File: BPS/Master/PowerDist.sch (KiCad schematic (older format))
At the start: 15 parts, among them J4 CarPowerConnector, U2 RI3-1205S, U3 NCP1117-3.3_SOT223

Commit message: Edited inductor choke in BPS master.
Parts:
- L1: footprint Inductor_SMD:L_0805_2012Metric -> UTSVT_BPS:SRF0905A; symbol Device:L -> utsvt-bps:SRF0905-100Y
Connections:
- wire segments 56 -> 64
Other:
- moved on the sheet: C16, TP1, TP15
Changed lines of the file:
@@
 L utsvt-connectors:CarPowerConnector J4
 U 1 1 5C35F236
-P 2800 3400
-F 0 "J4" H 2850 3750 60  0000 C CNN
-F 1 "CarPowerConnector" H 2500 3650 60  0000 C CNN
-F 2 "UTSVT_Connectors:Molex_MicroFit3.0_1x2xP3.00mm_PolarizingPeg_Vertical" H 2800 3400 60  0001 C CNN
-F 3 "" H 2800 3400 60  0001 C CNN
-	1    2800 3400
-	1    0    0    -1
-$EndComp
-Wire Wire Line
-	3100 3300 3150 3300
-Wire Wire Line
-	3100 3500 3150 3500
-Wire Wire Line
-	3150 3500 3150 3600
+P 2100 3400
+F 0 "J4" H 2150 3750 60  0000 C CNN
+F 1 "CarPowerConnector" H 1800 3650 60  0000 C CNN
+F 2 "UTSVT_Connectors:Molex_MicroFit3.0_1x2xP3.00mm_PolarizingPeg_Vertical" H 2100 3400 60  0001 C CNN
+F 3 "" H 2100 3400 60  0001 C CNN
+	1    2100 3400
+	1    0    0    -1
+$EndComp
+Wire Wire Line
+	2400 3300 2450 3300
+Wire Wire Line
+	2400 3500 2450 3500
+Wire Wire Line
+	2450 3500 2450 3600
 $Comp
 L power:+12V #PWR034
 U 1 1 5C35F2D2
-P 3150 3150
-F 0 "#PWR034" H 3150 3000 50  0001 C CNN
-F 1 "+12V" H 3165 3323 50  0000 C CNN
-F 2 "" H 3150 3150 50  0001 C CNN
-F 3 "" H 3150 3150 50  0001 C CNN
-	1    3150 3150
-	1    0    0    -1
-$EndComp
-Connection ~ 3150 3600
-Wire Wire Line
-	3150 3600 3150 3650
+P 2450 3150
+F 0 "#PWR034" H 2450 3000 50  0001 C CNN
+F 1 "+12V" H 2465 3323 50  0000 C CNN
+F 2 "" H 2450 3150 50  0001 C CNN
+F 3 "" H 2450 3150 50  0001 C CNN
+	1    2450 3150
+	1    0    0    -1
+$EndComp
+Connection ~ 2450 3600
+Wire Wire Line
+	2450 3600 2450 3650
 $Comp
 L Device:C C16
 U 1 1 5C35F7E4
-P 3400 3400
-F 0 "C16" H 3518 3446 50  0000 L CNN
-F 1 "4.7uF" H 3518 3355 50  0000 L CNN
-F 2 "Capacitor_SMD:C_0805_2012Metric" H 3438 3250 50  0001 C CNN
-F 3 "~" H 3400 3400 50  0001 C CNN
-	1    3400 3400
-	1    0    0    -1
-$EndComp
-Wire Wire Line
-	3150 3600 3400 3600
-$Comp
-L Device:L L1
-U 1 1 5C35FFD4
-P 3700 3200
-F 0 "L1" V 3890 3200 50  0000 C CNN
-F 1 "10uH" V 3799 3200 50  0000 C CNN
-F 2 "Inductor_SMD:L_0805_2012Metric" H 3700 3200 50  0001 C CNN
-F 3 "~" H 3700 3200 50  0001 C CNN
-	1    3700 3200
-	0    -1   -1   0
-$EndComp
-Wire Wire Line
-	3150 3150 3150 3200
-Wire Wire Line
-	3150 3200 3400 3200
-Connection ~ 3150 3200
-Wire Wire Line
-	3150 3200 3150 3300
-Wire Wire Line
-	3400 3250 3400 3200
-Connection ~ 3400 3200
-Wire Wire Line
-	3400 3200 3550 3200
-Wire Wire Line
-	3400 3550 3400 3600
-Connection ~ 3400 3600
-Wire Wire Line
-	3400 3600 4000 3600
-Wire Wire Line
-	4000 3200 3850 3200
+P 2700 3400
+F 0 "C16" H 2818 3446 50  0000 L CNN
+F 1 "4.7uF" H 2818 3355 50  0000 L CNN
+F 2 "Capacitor_SMD:C_0805_2012Metric" H 2738 3250 50  0001 C CNN
+F 3 "~" H 2700 3400 50  0001 C CNN
+	1    2700 3400
+	1    0    0    -1
+$EndComp
+Wire Wire Line
+	2450 3600 2700 3600
+Wire Wire Line
+	2450 3150 2450 3200
+Wire Wire Line
+	2450 3200 2700 3200
+Connection ~ 2450 3200
+Wire Wire Line
+	2450 3200 2450 3300
+Wire Wire Line
+	2700 3250 2700 3200
+Connection ~ 2700 3200
+Wire Wire Line
+	2700 3550 2700 3600
+Connection ~ 2700 3600
 Wire Wire Line
 	5200 3700 5200 3600
@@
 L Connector:TestPoint TP1
 U 1 1 5C37D606
-P 3400 3150
-F 0 "TP1" H 3400 3500 50  0000 L CNN
-F 1 "+12V_TP" H 3400 3400 50  0000 L CNN
-F 2 "TestPoint:TestPoint_Keystone_5005-5009_Compact" H 3600 3150 50  0001 C CNN
-F 3 "~" H 3600 3150 50  0001 C CNN
-	1    3400 3150
-	1    0    0    -1
-$EndComp
-Wire Wire Line
-	3400 3150 3400 3200
+P 2700 3150
+F 0 "TP1" H 2700 3500 50  0000 L CNN
+F 1 "+12V_TP" H 2700 3400 50  0000 L CNN
+F 2 "TestPoint:TestPoint_Keystone_5005-5009_Compact" H 2900 3150 50  0001 C CNN
+F 3 "~" H 2900 3150 50  0001 C CNN
+	1    2700 3150
+	1    0    0    -1
+$EndComp
+Wire Wire Line
+	2700 3150 2700 3200
 $Comp
 L Connector:TestPoint TP2
@@
 L power:GNDPWR #PWR036
 U 1 1 5C3F7204
-P 3150 3650
-F 0 "#PWR036" H 3150 3450 50  0001 C CNN
-F 1 "GNDPWR" H 3154 3496 50  0000 C CNN
-F 2 "" H 3150 3600 50  0001 C CNN
-F 3 "" H 3150 3600 50  0001 C CNN
-	1    3150 3650
+P 2450 3650
+F 0 "#PWR036" H 2450 3450 50  0001 C CNN
+F 1 "GNDPWR" H 2454 3496 50  0000 C CNN
+F 2 "" H 2450 3600 50  0001 C CNN
+F 3 "" H 2450 3600 50  0001 C CNN
+	1    2450 3650
 	1    0    0    -1
 $EndComp
@@
 L Connector:TestPoint TP15
 U 1 1 5C82CEA3
-P 3400 3650
-F 0 "TP15" H 3342 3677 50  0000 R CNN
-F 1 "GNDPWR_TP" H 3342 3768 50  0000 R CNN
-F 2 "TestPoint:TestPoint_Keystone_5005-5009_Compact" H 3600 3650 50  0001 C CNN
-F 3 "~" H 3600 3650 50  0001 C CNN
-	1    3400 3650
+P 2700 3650
+F 0 "TP15" H 2642 3677 50  0000 R CNN
+F 1 "GNDPWR_TP" H 2642 3768 50  0000 R CNN
+F 2 "TestPoint:TestPoint_Keystone_5005-5009_Compact" H 2900 3650 50  0001 C CNN
+F 3 "~" H 2900 3650 50  0001 C CNN
+	1    2700 3650
 	-1   0    0    1
 $EndComp
 Wire Wire Line
-	3400 3650 3400 3600
+	2700 3650 2700 3600
+Wire Wire Line
+	3800 3200 4000 3200
+Wire Wire Line
+	2700 3600 4000 3600
+$Comp
+L utsvt-bps:SRF0905-100Y L1
+U 1 1 5C35FFD4
+P 2950 3150
+F 0 "L1" H 3200 3450 50  0000 C CNN
+F 1 "10uH" H 3250 3350 50  0000 C CNN
+F 2 "UTSVT_BPS:SRF0905A" H 2950 3150 50  0001 C CNN
+F 3 "~" H 2950 3150 50  0001 C CNN
+	1    2950 3150
+	1    0    0    -1
+$EndComp
+Wire Wire Line
+	3800 3200 3800 3150
+Wire Wire Line
+	3800 3150 3750 3150
+Wire Wire Line
+	3750 3250 3800 3250
+Wire Wire Line
+	3800 3250 3800 3200
+Connection ~ 3800 3200
+Wire Wire Line
+	2950 3250 2900 3250
+Wire Wire Line
+	2900 3250 2900 3200
+Wire Wire Line
+	2900 3150 2950 3150
+Wire Wire Line
+	2700 3200 2900 3200
+Connection ~ 2900 3200
+Wire Wire Line
+	2900 3200 2900 3150
 $EndSCHEMATC

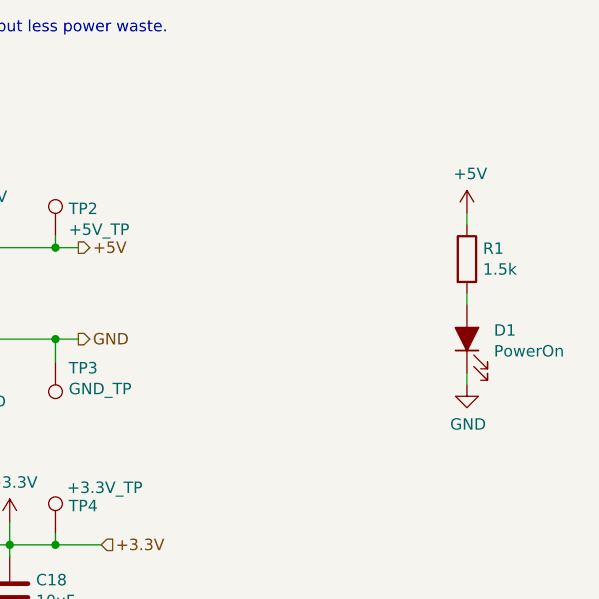
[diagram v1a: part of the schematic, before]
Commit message: Added labels to USB breakout.
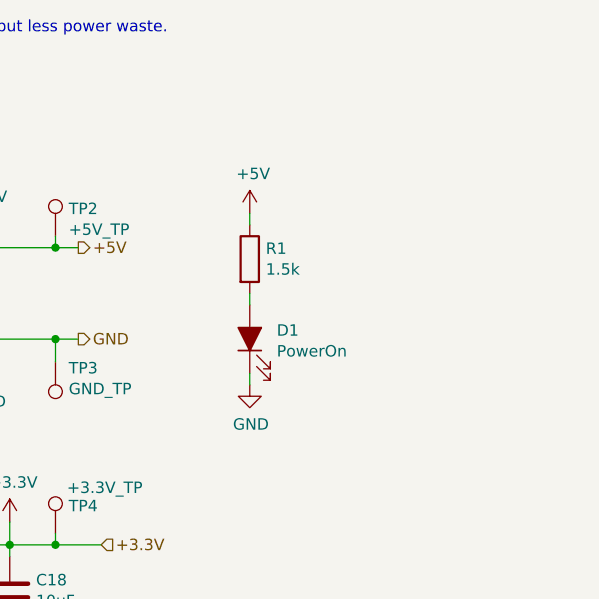
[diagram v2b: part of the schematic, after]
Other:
- moved on the sheet: D1, R1
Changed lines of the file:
@@
 L power:GND #PWR038
 U 1 1 5C58D746
-P 7300 3800
-F 0 "#PWR038" H 7300 3550 50  0001 C CNN
-F 1 "GND" H 7305 3627 50  0000 C CNN
-F 2 "" H 7300 3800 50  0001 C CNN
-F 3 "" H 7300 3800 50  0001 C CNN
-	1    7300 3800
+P 6350 3800
+F 0 "#PWR038" H 6350 3550 50  0001 C CNN
+F 1 "GND" H 6355 3627 50  0000 C CNN
+F 2 "" H 6350 3800 50  0001 C CNN
+F 3 "" H 6350 3800 50  0001 C CNN
+	1    6350 3800
 	1    0    0    -1
 $EndComp
@@
 L Device:LED_ALT D1
 U 1 1 5C58D83E
-P 7300 3600
-F 0 "D1" V 7338 3482 50  0000 R CNN
-F 1 "PowerOn" V 7247 3482 50  0000 R CNN
-F 2 "LED_SMD:LED_0805_2012Metric" H 7300 3600 50  0001 C CNN
-F 3 "~" H 7300 3600 50  0001 C CNN
-F 4 "Green" V 7300 3600 50  0001 C CNN "Color"
-F 5 "APTD2012LCGCK" V 7300 3600 50  0001 C CNN "P/N"
-	1    7300 3600
+P 6350 3600
+F 0 "D1" V 6388 3482 50  0000 R CNN
+F 1 "PowerOn" V 6297 3482 50  0000 R CNN
+F 2 "LED_SMD:LED_0805_2012Metric" H 6350 3600 50  0001 C CNN
+F 3 "~" H 6350 3600 50  0001 C CNN
+F 4 "Green" V 6350 3600 50  0001 C CNN "Color"
+F 5 "APTD2012LCGCK" V 6350 3600 50  0001 C CNN "P/N"
+	1    6350 3600
 	0    -1   -1   0
 $EndComp
@@
 L Device:R R1
 U 1 1 5C58D993
-P 7300 3250
-F 0 "R1" H 7370 3296 50  0000 L CNN
-F 1 "1.5k" H 7370 3205 50  0000 L CNN
-F 2 "Resistor_SMD:R_0805_2012Metric" V 7230 3250 50  0001 C CNN
-F 3 "~" H 7300 3250 50  0001 C CNN
-	1    7300 3250
+P 6350 3250
+F 0 "R1" H 6420 3296 50  0000 L CNN
+F 1 "1.5k" H 6420 3205 50  0000 L CNN
+F 2 "Resistor_SMD:R_0805_2012Metric" V 6280 3250 50  0001 C CNN
+F 3 "~" H 6350 3250 50  0001 C CNN
+	1    6350 3250
 	1    0    0    -1
 $EndComp
 Wire Wire Line
-	7300 3800 7300 3750
+	6350 3800 6350 3750
 Wire Wire Line
-	7300 3450 7300 3400
+	6350 3450 6350 3400
 $Comp
 L power:+5V #PWR033
 U 1 1 5C58FEF6
-P 7300 3050
-F 0 "#PWR033" H 7300 2900 50  0001 C CNN
-F 1 "+5V" H 7315 3223 50  0000 C CNN
-F 2 "" H 7300 3050 50  0001 C CNN
-F 3 "" H 7300 3050 50  0001 C CNN
-	1    7300 3050
+P 6350 3050
+F 0 "#PWR033" H 6350 2900 50  0001 C CNN
+F 1 "+5V" H 6365 3223 50  0000 C CNN
+F 2 "" H 6350 3050 50  0001 C CNN
+F 3 "" H 6350 3050 50  0001 C CNN
+	1    6350 3050
 	1    0    0    -1
 $EndComp
 Wire Wire Line
-	7300 3050 7300 3100
+	6350 3050 6350 3100
 $Comp
 L power:GND #PWR037

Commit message: Changed capacitor value for 3.3V regulator in BPS master.
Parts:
- C17: value 0.1uF -> 10uF
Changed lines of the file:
@@
 P 4300 4700
 F 0 "C17" H 4415 4746 50  0000 L CNN
-F 1 "0.1uF" H 4415 4655 50  0000 L CNN
+F 1 "10uF" H 4415 4655 50  0000 L CNN
 F 2 "Capacitor_SMD:C_0805_2012Metric" H 4338 4550 50  0001 C CNN
 F 3 "~" H 4300 4700 50  0001 C CNN
